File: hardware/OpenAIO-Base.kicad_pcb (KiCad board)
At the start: 6 copper layers, 35 x 35 mm, 254 parts, among them J15 5V, J16 5V, J17 5V, J18 5V, J20 5V, J21 5V, J24 5V, J25 5V, J27 5V, J28 5V, J29 5V, J31 5V, J32 5V, J33 5V, J90 Core_LGA, Q10 DOY180N03T, Q11 DOY180N03T, Q12 DOY180N03T, Q13 DOY180N03T, Q14 DOY180N03T, Q15 DOY180N03T, Q16 DOY180N03T, Q17 DOY180N03T, Q18 DOY180N03T, Q19 DOY180N03T, Q20 DOY180N03T, Q21 DOY180N03T, Q22 DOY180N03T, Q23 DOY180N03T, Q24 DOY180N03T, Q25 DOY180N03T, Q26 DOY180N03T, Q3 DOY180N03T, Q4 DOY180N03T, Q5 DOY180N03T, Q6 DOY180N03T, Q7 DOY180N03T, Q8 DOY180N03T, Q9 DOY180N03T, U12 SM06B-SRSS-TB(LF)(SN), U13 AT32F421G8U7, U14 NSG2065Q, U15 AT32F421G8U7, U16 NSG2065Q, U17 AT32F421G8U7, U18 NSG2065Q, U19 AT32F421G8U7, U20 NSG2065Q, U21 SX1281IMLTRT, U22 ESP32-C3, U23 TLV75533PDQNR, U24 AIO_outline, U25 INA186A3IDCKR, U3 LMR51430YFDDCR, U4 LMR51430YFDDCR, U7 LP5912-3.3DRVR, X2 CJ17-400001010B20

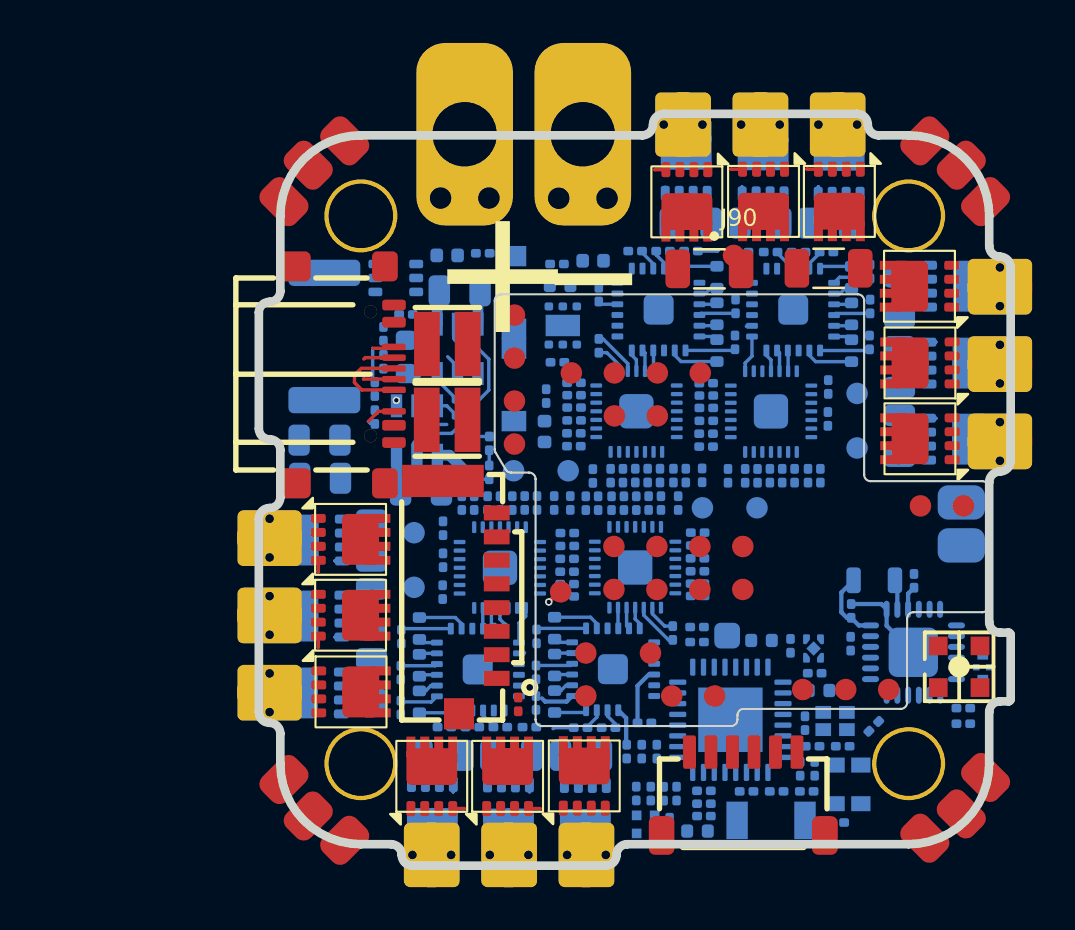
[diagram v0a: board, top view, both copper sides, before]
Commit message: OpenAIO: Core 3D model lives in the Core_LGA_land footprint, J90/J91 keep the lib nickname
Co-Authored-By: Claude Fable 5 <noreply@anthropic.com>
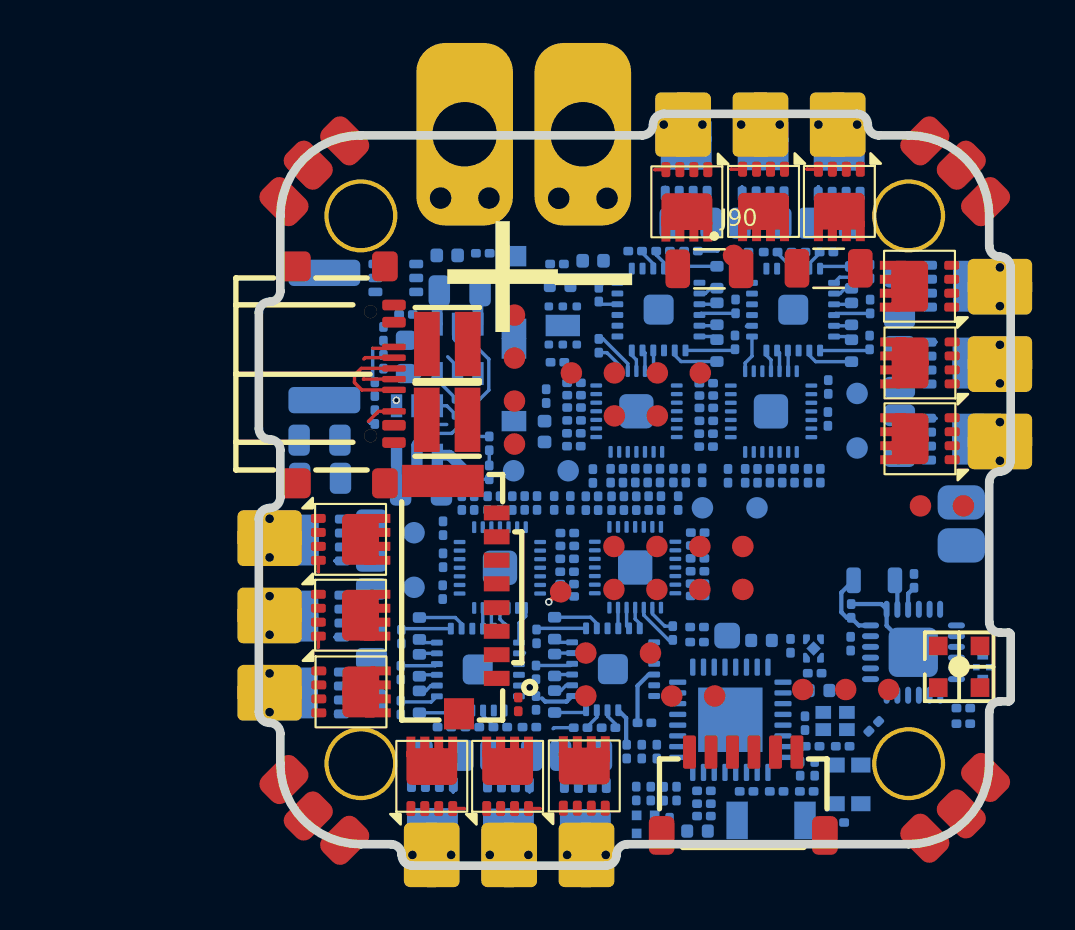
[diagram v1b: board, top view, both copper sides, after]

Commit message: OpenAIO: new marker test points TP29 (BUZZER-) and TP30 (+5V) on the Base; lga_apply only excludes the markers it consumed
Co-Authored-By: Claude Fable 5 <noreply@anthropic.com>
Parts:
- added TP29: TestPoint, TestPoint:TestPoint_Pad_D1.0mm, F.Cu at (50.0, 50.0)
- added TP30: TestPoint, TestPoint:TestPoint_Pad_D1.0mm, F.Cu at (60.0, 50.0)
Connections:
- C36 pad 1: +3.3V -> +3V3
- Card1 pad 4: +3.3V -> +3V3
- R34 pad 1: +3.3V -> +3V3
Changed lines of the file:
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@@
 		)
 	)
+	(footprint "TestPoint:TestPoint_Pad_D1.0mm"
+		(layer "F.Cu")
+		(at 60 50)
+		(descr "SMD pad as test Point, diameter 1.0mm")
+		(tags "test point SMD pad")
+		(property "Reference" "TP30"
+			(at 0 -1.448 0)
+			(layer "F.SilkS")
+			(effects
+				(font
+					(size 1 1)
+					(thickness 0.15)
+				)
+			)
+		)
+		(property "Value" "TestPoint"
+			(at 0 1.55 0)
+			(layer "F.Fab")
+			(effects
+				(font
+					(size 1 1)
+					(thickness 0.15)
+				)
+			)
+		)
+		(property "Datasheet" ""
+			(at 0 0 0)
+			(unlocked yes)
+			(layer "F.Fab")
+			(hide yes)
+			(effects
+				(font
+					(size 1.27 1.27)
+					(thickness 0.15)
+				)
+			)
+		)
+		(property "Description" ""
+			(at 0 0 0)
+			(unlocked yes)
+			(layer "F.Fab")
+			(hide yes)
+			(effects
+				(font
+					(size 1.27 1.27)
+					(thickness 0.15)
+				)
+			)
+		)
+		(attr exclude_from_pos_files exclude_from_bom)
+		(duplicate_pad_numbers_are_jumpers no)
+		(fp_circle
+			(center 0 0)
+			(end 0 0.7)
+			(stroke
+				(width 0.12)
+				(type solid)
+			)
+			(fill no)
+			(layer "F.SilkS")
+		)
+		(fp_circle
+			(center 0 0)
+			(end 1 0)
+			(stroke
+				(width 0.05)
+				(type solid)
+			)
+			(fill no)
+			(layer "F.CrtYd")
+		)
+		(fp_text user "${REFERENCE}"
+			(at 0 -1.45 0)
+			(layer "F.Fab")
+			(effects
+				(font
+					(size 1 1)
+					(thickness 0.15)
+				)
+			)
+		)
+		(pad "1" smd circle
+			(at 0 0)
+			(size 1 1)
+			(layers "F.Cu" "F.Mask")
+			(net "+5V")
+		)
+		(embedded_fonts no)
+	)
 	(footprint "OpenDrone:AIO_outline"
 		(layer "F.Cu")
@@
 			(layers "F.Cu" "F.Mask")
 			(roundrect_rratio 0.25)
-			(net "+3.3V")
+			(net "+3V3")
 			(pintype "passive")
 		)
@@
 		)
 	)
+	(footprint "TestPoint:TestPoint_Pad_D1.0mm"
+		(layer "F.Cu")
+		(at 50 50)
+		(descr "SMD pad as test Point, diameter 1.0mm")
+		(tags "test point SMD pad")
+		(property "Reference" "TP29"
+			(at 0 -1.448 0)
+			(layer "F.SilkS")
+			(effects
+				(font
+					(size 1 1)
+					(thickness 0.15)
+				)
+			)
+		)
+		(property "Value" "TestPoint"
+			(at 0 1.55 0)
+			(layer "F.Fab")
+			(effects
+				(font
+					(size 1 1)
+					(thickness 0.15)
+				)
+			)
+		)
+		(property "Datasheet" ""
+			(at 0 0 0)
+			(unlocked yes)
+			(layer "F.Fab")
+			(hide yes)
+			(effects
+				(font
+					(size 1.27 1.27)
+					(thickness 0.15)
+				)
+			)
+		)
+		(property "Description" ""
+			(at 0 0 0)
+			(unlocked yes)
+			(layer "F.Fab")
+			(hide yes)
+			(effects
+				(font
+					(size 1.27 1.27)
+					(thickness 0.15)
+				)
+			)
+		)
+		(attr exclude_from_pos_files exclude_from_bom)
+		(duplicate_pad_numbers_are_jumpers no)
+		(fp_circle
+			(center 0 0)
+			(end 0 0.7)
+			(stroke
+				(width 0.12)
+				(type solid)
+			)
+			(fill no)
+			(layer "F.SilkS")
+		)
+		(fp_circle
+			(center 0 0)
+			(end 1 0)
+			(stroke
+				(width 0.05)
+				(type solid)
+			)
+			(fill no)
+			(layer "F.CrtYd")
+		)
+		(fp_text user "${REFERENCE}"
+			(at 0 -1.45 0)
+			(layer "F.Fab")
+			(effects
+				(font
+					(size 1 1)
+					(thickness 0.15)
+				)
+			)
+		)
+		(pad "1" smd circle
+			(at 0 0)
+			(size 1 1)
+			(layers "F.Cu" "F.Mask")
+			(net "/Pads/BUZZER-")
+		)
+		(embedded_fonts no)
+	)
 	(footprint "Capacitor_SMD:C_1206_3216Metric"
 		(layer "F.Cu")
@@
 			(size 1.2 0.7)
 			(layers "F.Cu" "F.Mask" "F.Paste")
-			(net "+3.3V")
+			(net "+3V3")
 			(pinfunction "VDD_4")
 			(pintype "unspecified")
@@
 			(layers "B.Cu" "B.Mask")
 			(roundrect_rratio 0.25)
-			(net "+3.3V")
+			(net "+3V3")
 			(pintype "passive")
 		)

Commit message: OpenAIO: LGA 31 pins (+5V and BUZZER- added, stray GND removed), J91 follows the pattern centre automatically
Co-Authored-By: Claude Fable 5 <noreply@anthropic.com>
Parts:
- removed TP29, TP30: TestPoint, TestPoint:TestPoint_Pad_D1.0mm
- moved J90 1.39 mm to (80.2, 61.6)
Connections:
- J29 pad 1: /Pads/BUZZER- -> BUZZER-
- J90 pad 1: GND -> 10V_ENABLE
- J90 pad 10: GND -> USB_D-
- J90 pad 11: USB_D- -> +5V
- J90 pad 18: MOTOR1 -> BUZZER-
- J90 pad 19: MOTOR3 -> MOTOR1
- J90 pad 2: 10V_ENABLE -> CURR
- J90 pad 20: GND -> MOTOR3
- J90 pad 22: +BATT -> GND
- J90 pad 23: GND -> +BATT
- J90 pad 26: UART0_TX -> GND
- J90 pad 27: UART0_RX -> UART0_TX
- J90 pad 28: LED_STRIP -> UART0_RX
- J90 pad 29: UART1_RX -> LED_STRIP
- J90 pad 3: CURR -> SPI0.MISO
- J90 pad 30: UART1_TX -> UART1_RX
- J90 pad 4: SPI0.MISO -> SPI0.SCK
- J90 pad 5: SPI0.SCK -> SPI0.MOSI
- J90 pad 6: SPI0.MOSI -> FLASH_CS
- J90 pad 7: FLASH_CS -> USB_D+
- J90 pad 8: USB_D+ -> GND

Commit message: OpenAIO: LGA +10V pin added
Co-Authored-By: Claude Fable 5 <noreply@anthropic.com>
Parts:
- moved J29 2.19 mm to (91.2, 63.6), turned to 180 degrees
- moved J33 1.97 mm to (91.2, 61.6), turned to 180 degrees
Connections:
- J90 pad 10: USB_D- -> GND
- J90 pad 11: +5V -> USB_D-
- J90 pad 12: GND -> +5V
- J90 pad 14: MOTOR2 -> GND
- J90 pad 15: MOTOR4 -> MOTOR2
- J90 pad 16: GND -> MOTOR4
- J90 pad 18: BUZZER- -> GND
- J90 pad 19: MOTOR1 -> BUZZER-
- J90 pad 20: MOTOR3 -> MOTOR1
- J90 pad 21: GND -> MOTOR3
- J90 pad 23: +BATT -> GND
- J90 pad 24: GND -> +BATT
- J90 pad 27: UART0_TX -> GND
- J90 pad 28: UART0_RX -> UART0_TX
- J90 pad 29: LED_STRIP -> UART0_RX
- J90 pad 30: UART1_RX -> LED_STRIP
- J90 pad 31: UART1_TX -> UART1_RX
- J90 pad 7: USB_D+ -> +10V
- J90 pad 8: GND -> USB_D+

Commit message: OpenAIO: LGA +3.3V pin added
Co-Authored-By: Claude Fable 5 <noreply@anthropic.com>
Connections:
- J90 pad 11: USB_D- -> GND
- J90 pad 12: +5V -> USB_D-
- J90 pad 13: GND -> +5V
- J90 pad 15: MOTOR2 -> GND
- J90 pad 16: MOTOR4 -> MOTOR2
- J90 pad 17: GND -> MOTOR4
- J90 pad 19: BUZZER- -> GND
- J90 pad 20: MOTOR1 -> BUZZER-
- J90 pad 21: MOTOR3 -> MOTOR1
- J90 pad 22: GND -> MOTOR3
- J90 pad 24: +BATT -> GND
- J90 pad 25: GND -> +BATT
- J90 pad 28: UART0_TX -> GND
- J90 pad 29: UART0_RX -> UART0_TX
- J90 pad 30: LED_STRIP -> UART0_RX
- J90 pad 31: UART1_RX -> LED_STRIP
- J90 pad 32: UART1_TX -> UART1_RX
- J90 pad 8: USB_D+ -> +3.3V
- J90 pad 9: GND -> USB_D+

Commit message: OpenAIO: LGA +4v5 pin added
Co-Authored-By: Claude Fable 5 <noreply@anthropic.com>
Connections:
- J90 pad 12: USB_D- -> +4v5
- J90 pad 13: +5V -> USB_D-
- J90 pad 14: GND -> +5V
- J90 pad 16: MOTOR2 -> GND
- J90 pad 17: MOTOR4 -> MOTOR2
- J90 pad 18: GND -> MOTOR4
- J90 pad 20: BUZZER- -> GND
- J90 pad 21: MOTOR1 -> BUZZER-
- J90 pad 22: MOTOR3 -> MOTOR1
- J90 pad 23: GND -> MOTOR3
- J90 pad 25: +BATT -> GND
- J90 pad 26: GND -> +BATT
- J90 pad 29: UART0_TX -> GND
- J90 pad 30: UART0_RX -> UART0_TX
- J90 pad 31: LED_STRIP -> UART0_RX
- J90 pad 32: UART1_RX -> LED_STRIP
- J90 pad 33: UART1_TX -> UART1_RX

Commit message: OpenAIO: Base and Core routing progress; README states the two-board design as drawn
Co-Authored-By: Claude Fable 5 <noreply@anthropic.com>
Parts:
- moved R22 1.88 mm to (71.2, 58.4), turned to 90 degrees
- moved D5 1.42 mm to (71.2, 56.8), turned to -90 degrees
- moved C105 0.55 mm to (83.9, 50.6)
- moved R105 0.23 mm to (78.7, 59.1)
- moved R107 0.23 mm to (78.7, 58.5)
- moved R81 0.07 mm to (80.1, 51.0)
- moved C64 0.06 mm to (80.4, 49.9)
- moved U25 0.06 mm to (64.3, 51.1)
- turned R48 to 180 degrees
- turned R50 to 180 degrees
- turned R67 to 180 degrees
- turned R69 to 180 degrees
- turned R80 to 180 degrees
- turned R86 to 0 degrees
- turned R88 to 0 degrees
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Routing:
- net GND: track 17.7 -> 61.3 mm, vias 0 -> 231
- net +3V3: track 5.47 -> 24.3 mm, vias 0 -> 7
- net +10V: track 4.58 -> 15.8 mm, vias 0 -> 7
- net Net-(U4-FB): track 0.00 -> 5.88 mm
- net +5V_USB: track 0.00 -> 5.76 mm, vias 0 -> 7
- net +4v5: track 0.00 -> 4.99 mm
- net /ESC3/AL: track 0.00 -> 3.96 mm
- net /ESC2/FBCOMMON: track 0.00 -> 3.61 mm, vias 0 -> 2
- net /ESC3/FBCOMMON: track 0.00 -> 3.36 mm, vias 0 -> 2
- net Net-(U17-PB4): track 0.00 -> 3.35 mm
- net Net-(U19-PA13): track 0.00 -> 3.32 mm
- net Net-(U13-PA13): track 0.00 -> 3.30 mm
- net /ESC2/CL: track 0.00 -> 3.29 mm, vias 0 -> 2
- net /ESC1/FBCOMMON: track 0.00 -> 3.25 mm, vias 0 -> 2
- net Net-(Q20-G): track 0.32 -> 3.52 mm
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- added copper zone on B.Cu, net +5V
- added copper zone on B.Cu, net Net-(U4-SW)
